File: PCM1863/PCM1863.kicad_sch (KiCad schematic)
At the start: 55 parts, among them IC2 NCP163ASN330T1G, IC3 NCP163ASN330T1G, J1 Conn_01x04_Pin, J2 Conn_01x04_Pin, J3 Conn_01x04_Pin, J5 Conn_01x04_Pin, J6 Conn_01x10_Pin, U1 PCM1863, Y1 ASE-24.000MHZ-ET

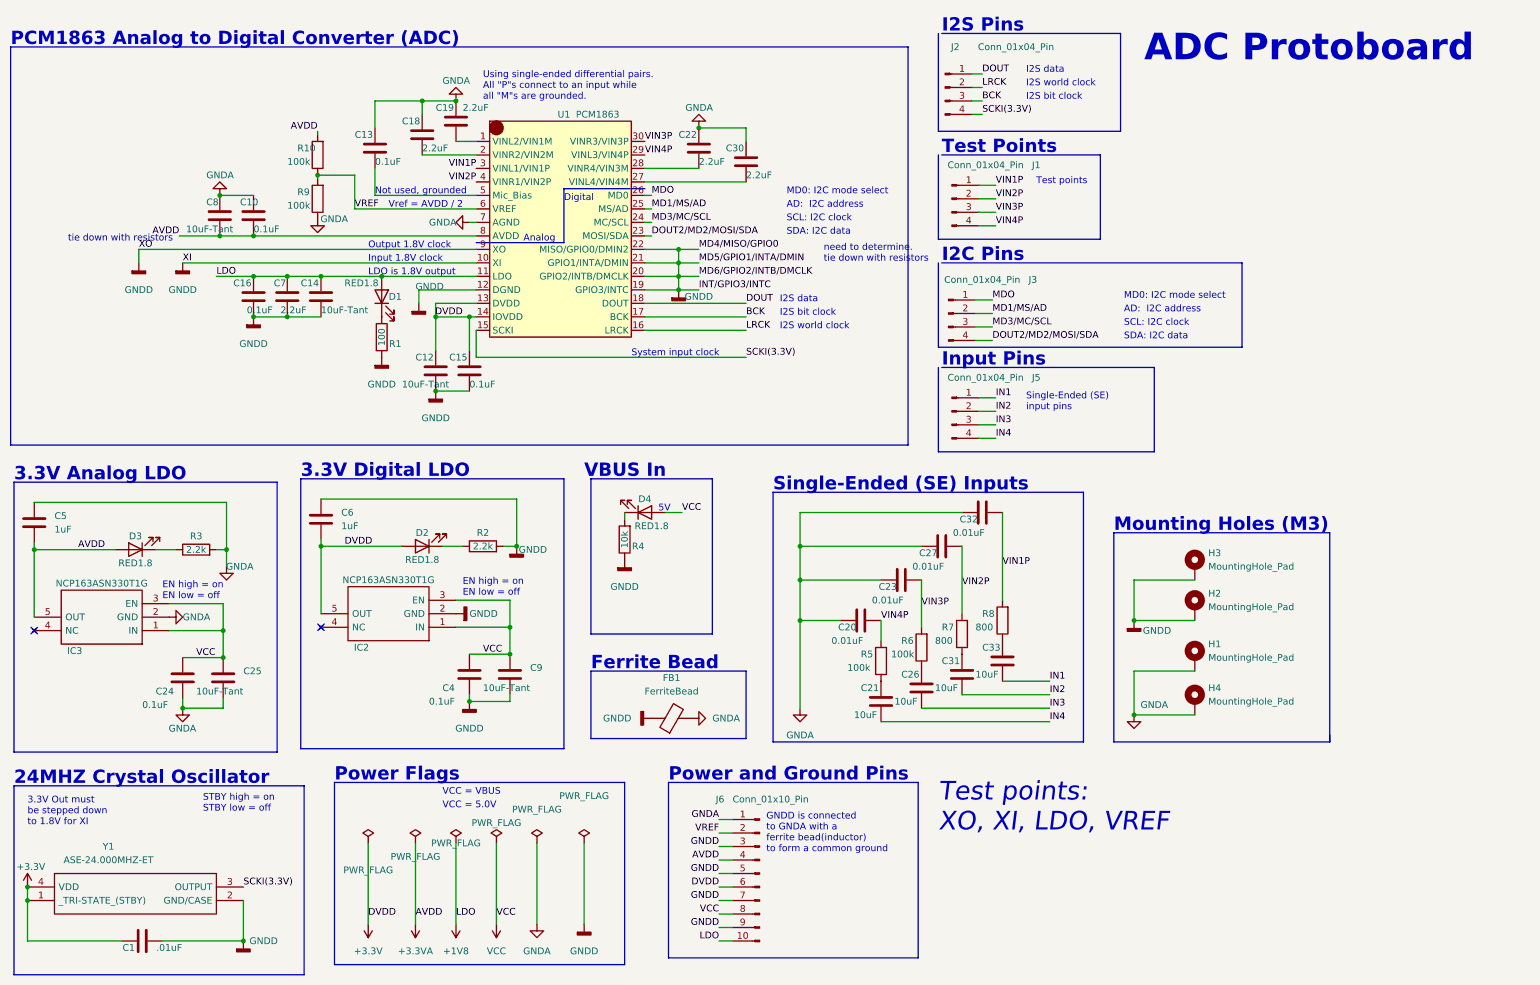
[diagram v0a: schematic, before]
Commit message: adc update to match IO
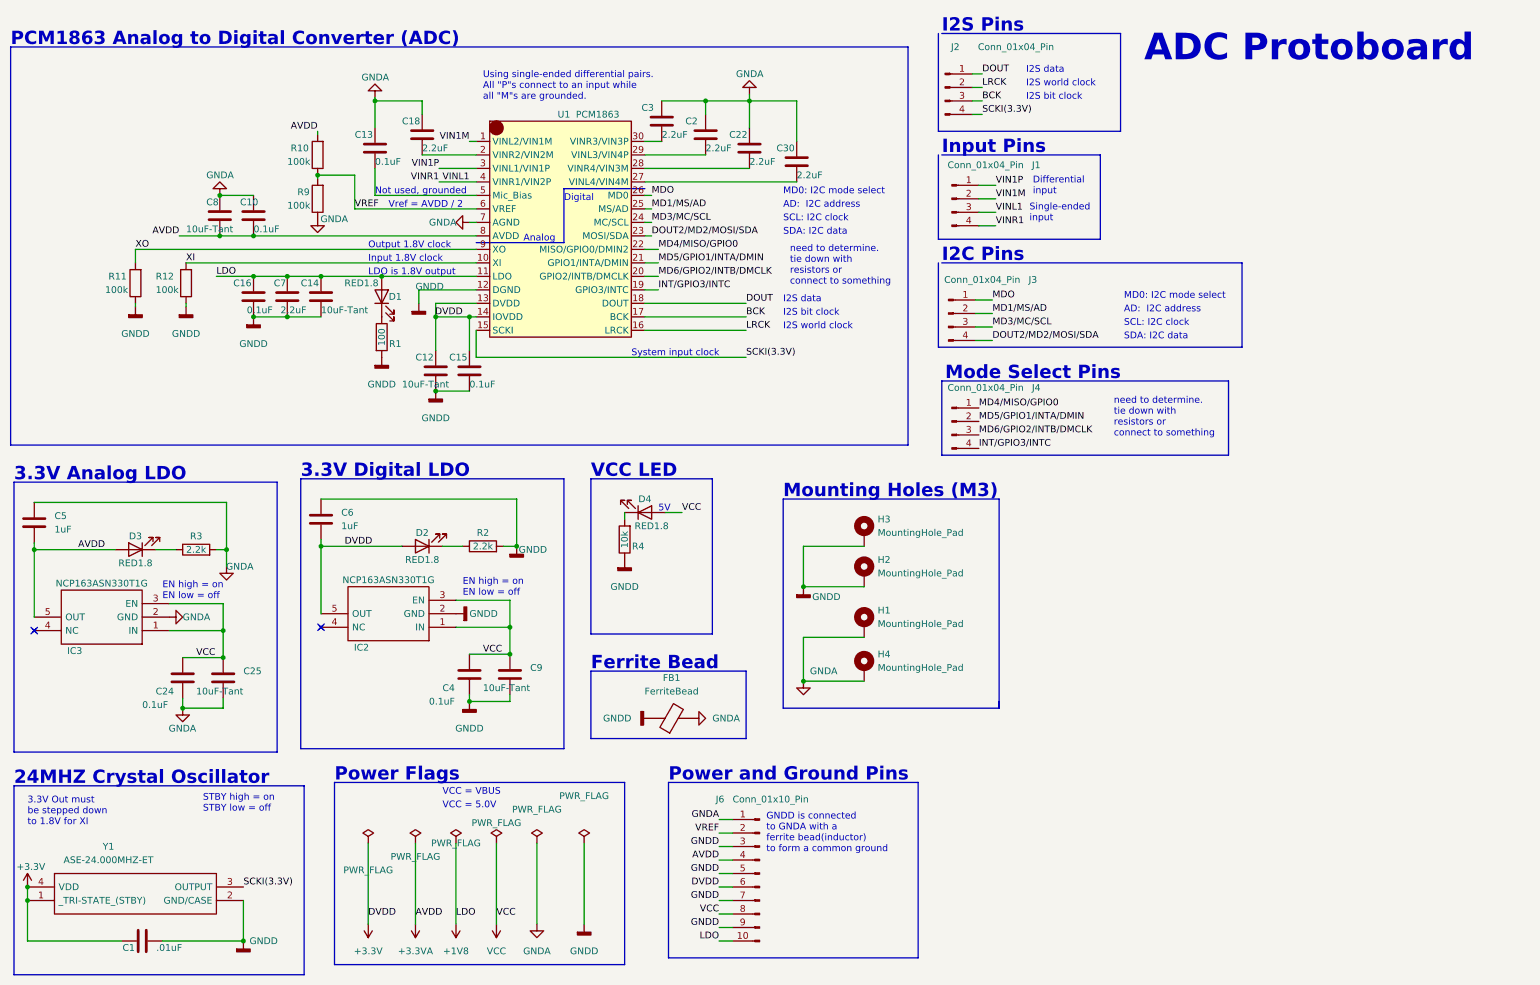
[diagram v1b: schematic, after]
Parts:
- removed C19: 2.2uF, Capacitor_SMD:C_0603_1608Metric_Pad1.08x0.95mm_HandSolder, symbol Device:C
- removed C20, C23, C27, C32: 0.01uF, Capacitor_SMD:C_0603_1608Metric_Pad1.08x0.95mm_HandSolder, symbol Device:C
- removed C21, C26, C31, C33: 10uF, Capacitor_SMD:C_0603_1608Metric_Pad1.08x0.95mm_HandSolder, symbol Device:C
- removed J5: Conn_01x04_Pin, Connector_PinHeader_2.54mm:PinHeader_1x04_P2.54mm_Vertical, symbol Connector:Conn_01x04_Pin
- removed R5, R6: 100k, Resistor_SMD:R_0603_1608Metric_Pad0.98x0.95mm_HandSolder, symbol Device:R
- removed R7, R8: 800, Resistor_SMD:R_0603_1608Metric_Pad0.98x0.95mm_HandSolder, symbol Device:R
- added C2, C3: 2.2uF, Capacitor_SMD:C_0603_1608Metric_Pad1.08x0.95mm_HandSolder, symbol Device:C
- added J4: Conn_01x04_Pin, Connector_PinHeader_2.54mm:PinHeader_1x04_P2.54mm_Vertical, symbol Connector:Conn_01x04_Pin
- added R11, R12: 100k, Resistor_SMD:R_0603_1608Metric_Pad0.98x0.95mm_HandSolder, symbol Device:R
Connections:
- net GNDA: now also C2.1, C3.1
- net GNDD: now also R11.1, R12.1; no longer U1.10 (XI), U1.19 (GPIO3/INTC), U1.20 (GPIO2/INTB/DMCLK), U1.21 (GPIO1/INTA/DMIN), U1.22 (MISO/GPIO0/DMIN2), U1.9 (XO)
- net VIN1M: now reaches U1.1 (VINL2/VIN1M)
- net VIN1M: now also J1.2 (Pin_2)
- net VIN2P renamed VINL1
- net VINL1: now also J1.3 (Pin_3), J1.4 (Pin_4); no longer J1.2 (Pin_2)
- net VIN3P: no longer names the net of U1.30 (VINR3/VIN3P)
- net VIN3P: now also C3.2; no longer J1.3 (Pin_3)
- net VIN4P: no longer names the net of U1.29 (VINL3/VIN4P)
- net VIN4P: now also C2.2; no longer J1.4 (Pin_4)
- new net INT/GPIO3/INTC: J4.4 (Pin_4), U1.19 (GPIO3/INTC)
- new net MD4/MISO/GPIO0: J4.1 (Pin_1), U1.22 (MISO/GPIO0/DMIN2)
- new net MD5/GPIO1/INTA/DMIN: J4.2 (Pin_2), U1.21 (GPIO1/INTA/DMIN)
- new net MD6/GPIO2/INTB/DMCLK: J4.3 (Pin_3), U1.20 (GPIO2/INTB/DMCLK)
- new net XI: R12.2, U1.10 (XI)
- new net XO: R11.2, U1.9 (XO)
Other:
- note added: "Differential input"
- note added: "Mode Select Pins"
- note added: "Single-ended input"
- note added: "VCC LED"
- note added: "need to determine. tie down with resistors or connect to something"
- note removed: "Single-Ended (SE) Inputs"
- note removed: "Single-Ended (SE) input pins"
- note removed: "Test Points"
- note removed: "Test points"
- note removed: "Test points: XO, XI, LDO, VREF"
- note removed: "VBUS In"
- note removed: "need to determine. tie down with resistors"
- note removed: "tie down with resistors"
- moved on the sheet: C22, C30, H1, H2, H3, H4

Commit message: plz work
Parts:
- removed H1, H2, H3, H4: MountingHole_Pad, MountingHole:MountingHole_3.2mm_M3_Pad, symbol Mechanical:MountingHole_Pad
- J2: footprint (none) -> Connector_PinHeader_2.54mm:PinHeader_1x04_P2.54mm_Vertical
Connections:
- net +1V8: now also J6.8 (Pin_8); no longer J6.10 (Pin_10)
- net +3.3VA: now also J6.10 (Pin_10); no longer J6.4 (Pin_4)
- net +3V3: now also J6.2 (Pin_2); no longer J6.6 (Pin_6)
- net GNDA: now also J6.3 (Pin_3); no longer J6.1 (Pin_1)
- net GNDD: now also J6.1 (Pin_1); no longer J6.3 (Pin_3)
- net VCC: now also J6.6 (Pin_6); no longer J6.8 (Pin_8)
- net VIN1P: now also J1.3 (Pin_3)
- net VREF: now also J6.4 (Pin_4); no longer J6.2 (Pin_2)
- net VINL1 renamed VINR1
- net VINR1: no longer J1.3 (Pin_3)
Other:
- note removed: "Mounting Holes (M3)"

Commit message: fixed bitwise operations
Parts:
- added J5: Conn_01x02_Pin, symbol Connector:Conn_01x02_Pin
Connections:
- net SCKI(3.3V): now also J5.1 (Pin_1); no longer Y1.3 (OUTPUT)
- new net: J5.2 (Pin_2), Y1.3 (OUTPUT)
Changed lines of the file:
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@@
+    (stroke (width 0) (type default))
+  )
+  (wire (pts (xy 59.055 172.085) (xy 59.055 175.895))
     (stroke (width 0) (type default))
   )
@@
     (effects (font (size 1.27 1.27)) (justify left bottom))
   )
-  (label "SCKI(3.3V)" (at 59.055 175.895 0) (fields_autoplaced)
+  (label "SCKI(3.3V)" (at 59.055 169.545 0) (fields_autoplaced)
     (effects (font (size 1.27 1.27)) (justify left bottom))
   )
@@
         )
       )
+    )
+  )
+  (symbol (lib_id "Connector:Conn_01x02_Pin") (at 53.975 169.545 0) (unit 1)
+    (in_bom yes) (on_board yes) (dnp no)
+    (property "Reference" "J5" (at 54.61 165.1 0)
+      (effects (font (size 1.27 1.27)))
+    )
+    (property "Value" "Conn_01x02_Pin" (at 44.45 164.465 0)
+      (effects (font (size 1.27 1.27)))
+    )
+    (property "Footprint" "" (at 53.975 169.545 0)
+      (effects (font (size 1.27 1.27)) hide)
+    )
+    (property "Datasheet" "~" (at 53.975 169.545 0)
+      (effects (font (size 1.27 1.27)) hide)
+    )
+    (pin "1")
+    (pin "2")
+    (instances
+      (project "PCM1863"
+        (path "/3988ee5d-eab1-4284-8462-2f0088830500"
+          (reference "J5") (unit 1)
+        )
+      )
